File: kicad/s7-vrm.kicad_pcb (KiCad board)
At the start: 2 copper layers, 58.4 x 53 mm, 32 parts, among them J1 Conn_02x15_Row_Letter_First, Q1 Q_NPN_BEC, Q2 Q_NMOS_GDS, Q3 Q_NMOS_GDS, SW1 SW_DIP_x04, U1 NCP1579

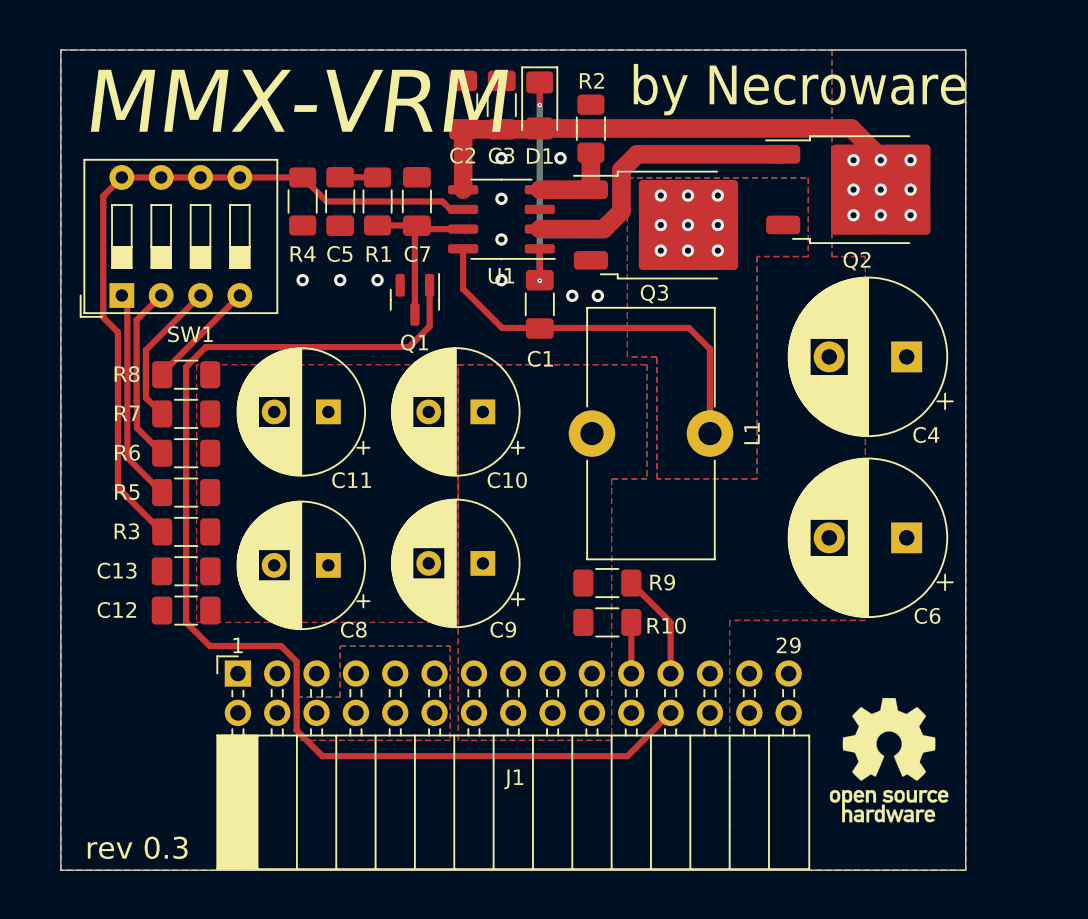
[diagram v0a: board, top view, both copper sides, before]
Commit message: Revision 0.4
- Added optional 1uF capacitors on input and output
- Increased the size of the inductor pins for SMD option
- Minor layout fixes
- Updated silk layer, logos etc.
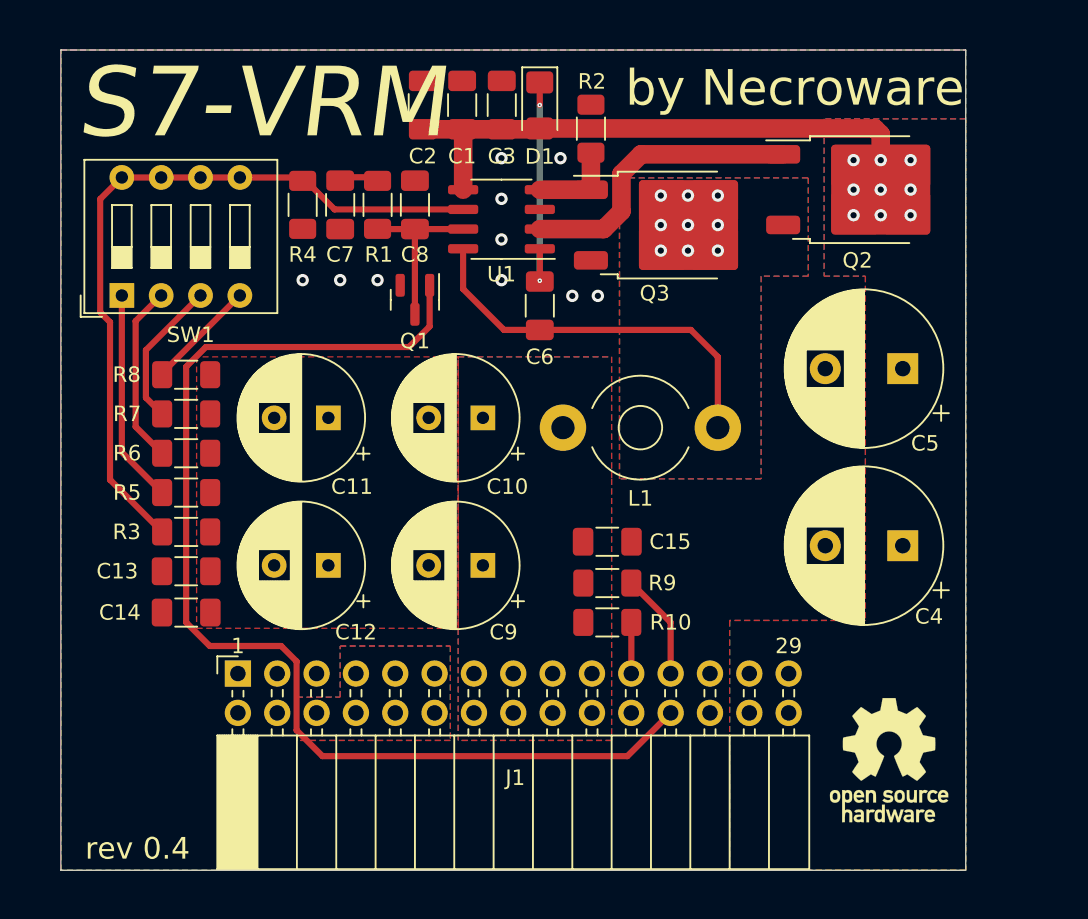
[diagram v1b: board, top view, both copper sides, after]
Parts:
- added C14: 4.7u, Capacitor_SMD:C_1206_3216Metric_Pad1.33x1.80mm_HandSolder, F.Cu at (129.0, 115.3)
- added C15: 10u, Capacitor_SMD:C_1206_3216Metric_Pad1.33x1.80mm_HandSolder, F.Cu at (156.2, 110.7)
- added G***: LOGO, s7-vrm:nw-logo, B.Cu at (143.1, 86.6)
- added G***: LOGO, s7-vrm:cc-by-sa-logo, B.Cu at (143.3, 96.1)
- C1: value 0.1u -> 10u
- C12: value 4.7u -> 1000u; footprint Capacitor_SMD:C_1206_3216Metric_Pad1.33x1.80mm_HandSolder -> Capacitor_THT:CP_Radial_D8.0mm_P3.50mm
- C5: value 22n -> 3300u; footprint Capacitor_SMD:C_1206_3216Metric_Pad1.33x1.80mm_HandSolder -> Capacitor_THT:CP_Radial_D10.0mm_P5.00mm
- C6: value 3300u -> 0.1u; footprint Capacitor_THT:CP_Radial_D10.0mm_P5.00mm -> Capacitor_SMD:C_1206_3216Metric_Pad1.33x1.80mm_HandSolder
- C7: value 220p -> 220nF
- C8: value 1000u -> 39p; footprint Capacitor_THT:CP_Radial_D8.0mm_P3.50mm -> Capacitor_SMD:C_1206_3216Metric_Pad1.33x1.80mm_HandSolder
- L1: value 2,5uH -> 2,5µH; footprint Inductor_THT:L_Toroid_Vertical_L16.0mm_W8.0mm_P7.62mm -> Inductor_THT:L_Toroid_Horizontal_D6.5mm_P10.00mm_Diameter7-5mm_Amidon-T25
- moved C5 37.9 mm to (175.3, 99.6), turned to 180 degrees
- moved C6 28.0 mm to (151.8, 95.5), turned to -90 degrees
- moved C8 23.9 mm to (143.8, 89.0), turned to 90 degrees
- moved C1 13.8 mm to (146.8, 82.5), turned to 90 degrees
- moved C4 12.2 mm to (175.3, 111.0)
- moved C12 9.64 mm to (138.2, 112.3)
- moved C7 4.96 mm to (138.9, 89.0), turned to -90 degrees
- moved C2 2.61 mm to (144.3, 82.5)
- moved L1 0.64 mm to (163.3, 103.4), turned to 180 degrees
- moved C10 0.38 mm to (148.2, 102.7)
- moved C11 0.38 mm to (138.2, 102.7)
- moved R1 0.22 mm to (141.4, 89.0)
- moved R4 0.22 mm to (136.5, 89.0)
- moved C9 0.13 mm to (148.2, 112.3)
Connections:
- C1 pad 1: /BST -> +5V
- C1 pad 2: /PHASE -> GND
- C5 pad 1: Net-(C5-Pad1) -> +5V
- C6 pad 1: +5V -> /BST
- C6 pad 2: GND -> /PHASE
- C7 pad 1: /COMP -> Net-(C7-Pad1)
- C8 pad 1: VCORE -> /COMP
- R1 pad 2: Net-(C5-Pad1) -> Net-(C7-Pad1)
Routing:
- net +5V: track 33.7 -> 37.2 mm
- net Net-(C7-Pad1): track 0.00 -> 2.42 mm
- net Net-(C5-Pad1): track 2.42 -> 0.00 mm
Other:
- board text added: "${TITLE}"
- board text removed: "MMX-VRM"

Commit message: Updated logos, readme and photo
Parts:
- G***: moved to F.Cu
- moved G*** 32.8 mm to (126.2, 124.2), turned to 90 degrees
- moved G*** 26.6 mm to (169.6, 88.6)
- moved REF** 1.66 mm to (174.5, 123.2)

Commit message: Layout improvements
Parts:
- R3: value 3K -> 1K
- R4: value 1K -> 3K
- moved R4 22.4 mm to (129.0, 110.1), turned to 180 degrees
- moved R3 22.4 mm to (136.4, 89.0), turned to -90 degrees
- moved C13 2.67 mm to (129.0, 115.3)
- moved C14 2.60 mm to (129.0, 112.7)
- moved C1 2.54 mm to (144.3, 82.5)
- moved C2 2.54 mm to (146.8, 82.5)
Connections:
- R3 pad 1: VCORE -> FB
- R3 pad 2: FB -> GND
- R4 pad 1: FB -> VCORE
- R4 pad 2: GND -> FB
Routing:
- net /PHASE: track 25.4 -> 23.3 mm

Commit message: Fixed BOM in readme, fixed part numbers in schematics
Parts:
- C7: value 220nF -> 220n
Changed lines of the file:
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@@
         (effects (font (size 1 1) (thickness 0.15)))
     )
-    (fp_text value "220nF" (at 0 1.85 90) (layer "F.Fab")
+    (fp_text value "220n" (at 0 1.85 90) (layer "F.Fab")
         (effects (font (size 1 1) (thickness 0.15)))
     )

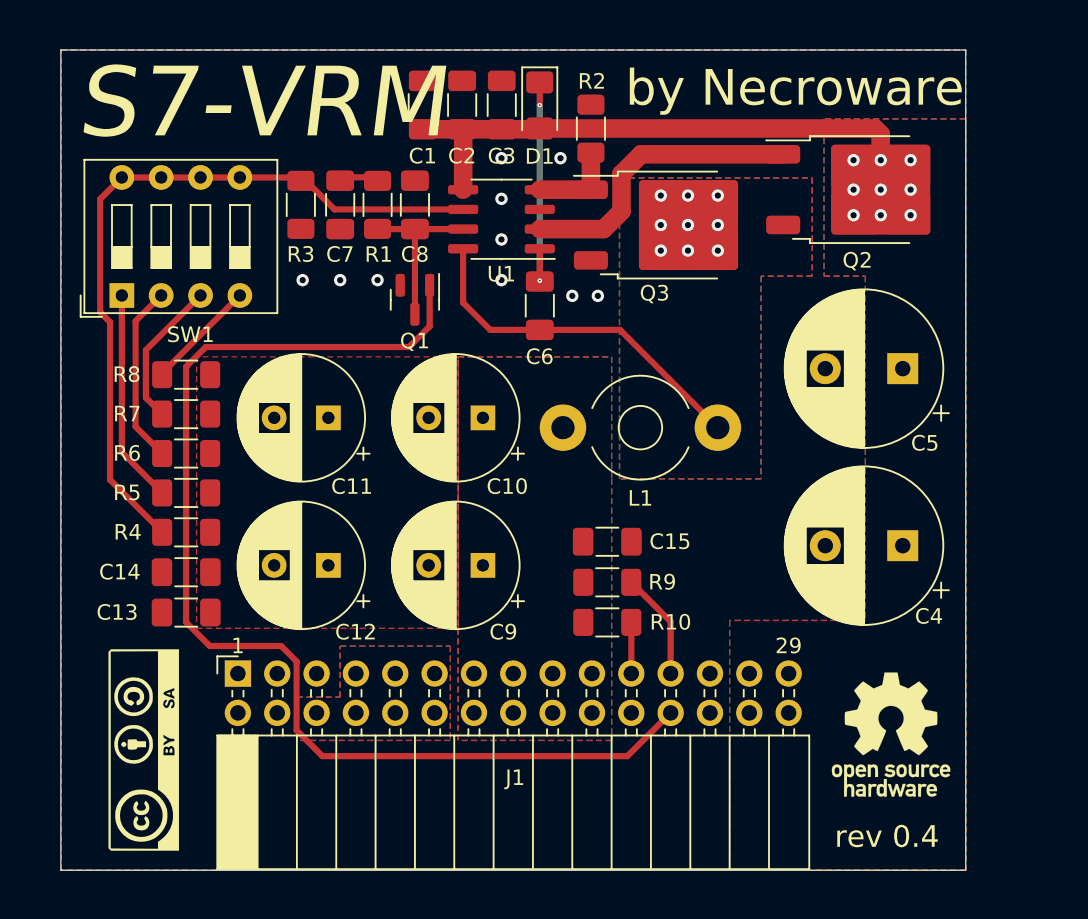
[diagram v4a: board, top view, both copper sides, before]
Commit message: Layout improvements, added slits for the clips
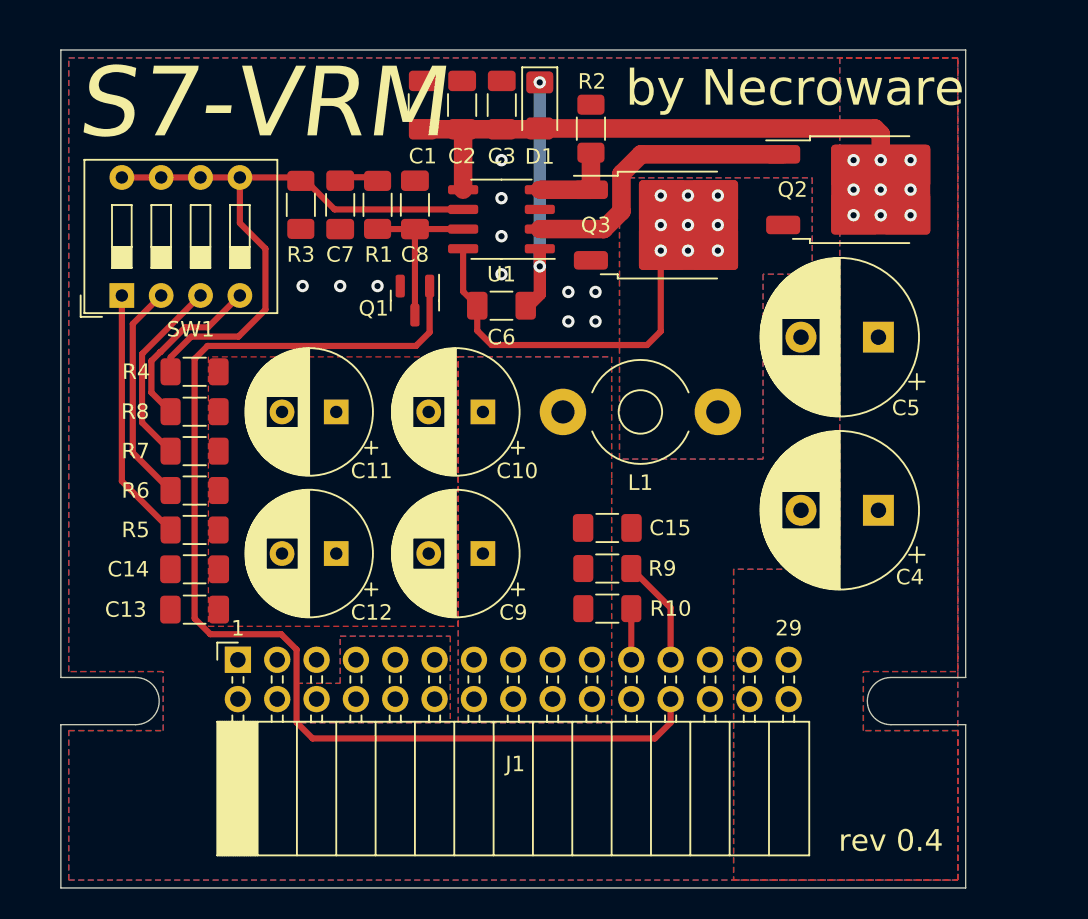
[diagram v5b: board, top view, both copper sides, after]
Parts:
- removed the G*** at (169.6, 88.6)
- C13, C3, C6: value 0.1u -> 100n
- G***, REF**: moved to B.Cu
- moved G*** 55.2 mm to (171.3, 92.3), turned to 180 degrees
- moved REF** 38.6 mm to (171.3, 84.7), turned to 180 degrees
- moved R4 10.4 mm to (129.5, 99.8)
- moved C4 2.77 mm to (173.7, 108.7)
- moved C5 2.57 mm to (173.7, 97.5)
- moved C6 2.47 mm to (149.4, 95.5), turned to 180 degrees
- moved R5 2.45 mm to (129.5, 110.0)
- moved R6 2.45 mm to (129.5, 107.4)
- moved R7 2.45 mm to (129.5, 104.9)
- moved R8 2.45 mm to (129.5, 102.3)
- moved L1 1.02 mm to (163.3, 102.4)
- moved C12 0.92 mm to (138.7, 111.5)
- moved C15 0.89 mm to (156.2, 109.9)
- moved J1 0.89 mm to (132.3, 118.4)
- moved R10 0.89 mm to (156.2, 115.1)
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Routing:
- net FB: track 48.0 -> 40.4 mm
- net Net-(R8-Pad2): track 7.19 -> 11.3 mm
- net Net-(R7-Pad2): track 9.54 -> 12.4 mm
- net Net-(R6-Pad2): track 11.6 -> 14.4 mm
- net Net-(R5-Pad2): track 13.8 -> 16.4 mm
- net /BST: track 14.8 -> 15.9 mm
- net GND: vias 10 -> 11
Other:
- board size 58.4 x 53 mm -> 58.4 x 54.1 mm

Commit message: Updated parts and documenttion
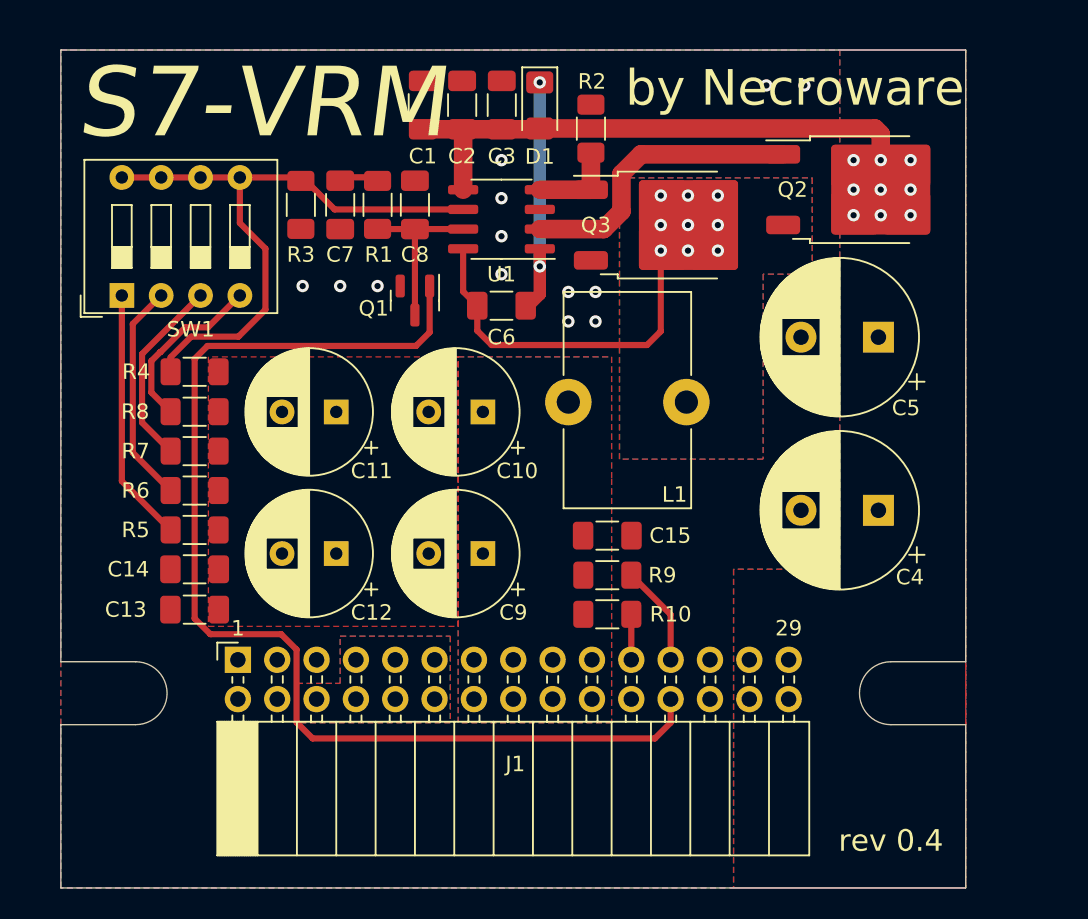
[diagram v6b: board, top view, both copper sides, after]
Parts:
- L1: value 2,5µH -> 3,3u; footprint Inductor_THT:L_Toroid_Horizontal_D6.5mm_P10.00mm_Diameter7-5mm_Amidon-T25 -> Inductor_THT:L_Toroid_Vertical_L16.0mm_W8.0mm_P7.62mm
- moved L1 2.13 mm to (161.3, 101.7), turned to -90 degrees
- moved C15 0.49 mm to (156.2, 110.3)
- moved R9 0.43 mm to (156.2, 112.9)
- moved R10 0.37 mm to (156.2, 115.4)
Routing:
- net GND: vias 11 -> 13
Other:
- outline, holes or cut-outs redrawn

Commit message: Increase PCB width slightly
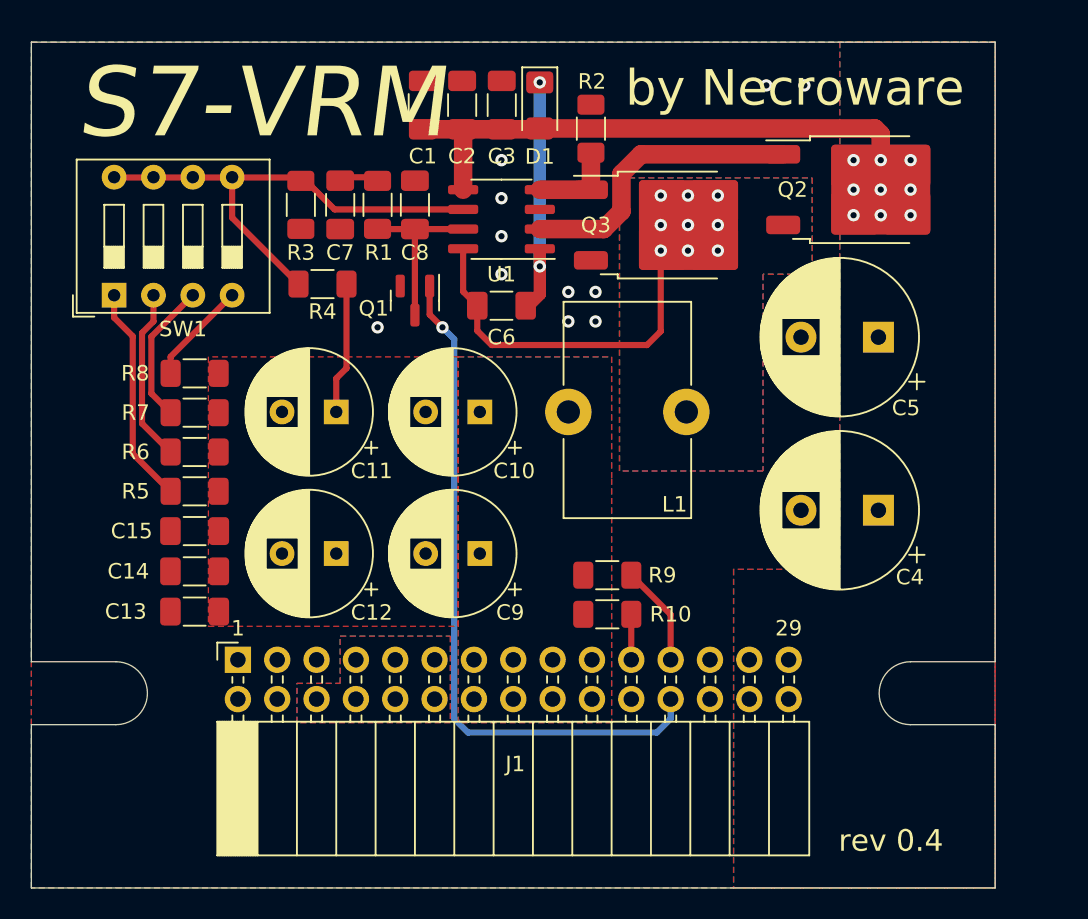
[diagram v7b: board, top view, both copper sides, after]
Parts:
- moved C15 26.6 mm to (129.5, 110.1), turned to 180 degrees
- moved R4 10.0 mm to (137.8, 94.1)
- moved R5 2.49 mm to (129.5, 107.5)
- moved R6 2.49 mm to (129.5, 104.9)
- moved R7 2.48 mm to (129.5, 102.4)
- moved R8 2.48 mm to (129.5, 99.9)
- moved L1 0.63 mm to (161.3, 102.4)
- moved SW1 0.50 mm to (124.3, 94.8)
- moved C10 0.20 mm to (148.0, 102.4)
- moved C9 0.20 mm to (148.0, 111.5)
- moved C14 0.13 mm to (129.5, 112.7)
- moved C13 0.13 mm to (129.5, 115.3)
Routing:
- net DISABLE: track 74.3 -> 44.6 mm, vias 0 -> 1
- net VCORE: track 0.00 -> 8.53 mm
- net FB: track 40.4 -> 32.1 mm
- net Net-(R8-Pad2): track 11.3 -> 6.69 mm
- net Net-(R6-Pad2): track 14.4 -> 11.2 mm
- net Net-(R7-Pad2): track 12.4 -> 9.21 mm
- net Net-(R5-Pad2): track 16.4 -> 14.2 mm
- net GND: vias 13 -> 11
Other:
- board size 58.4 x 54.1 mm -> 62.2 x 54.6 mm

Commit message: Take shorter input capacitor
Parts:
- C4, C5: value 3300u -> 2200u
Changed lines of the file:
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@@
     (descr "CP, Radial series, Radial, pin pitch=5.00mm, , diameter=10mm, Electrolytic Capacitor")
     (tags "CP Radial series Radial pin pitch 5.00mm  diameter 10mm Electrolytic Capacitor")
-    (property "LCSC" "C407862")
+    (property "LCSC" "C407963")
     (property "Sheetfile" "s7-vrm.kicad_sch")
     (property "Sheetname" "")
@@
         (effects (font (size 1 1) (thickness 0.15)))
     )
-    (fp_text value "3300u" (at 2.54 2.54) (layer "F.Fab")
+    (fp_text value "2200u" (at 2.54 2.54) (layer "F.Fab")
         (effects (font (size 1 1) (thickness 0.15)))
     )
@@
     (descr "CP, Radial series, Radial, pin pitch=5.00mm, , diameter=10mm, Electrolytic Capacitor")
     (tags "CP Radial series Radial pin pitch 5.00mm  diameter 10mm Electrolytic Capacitor")
-    (property "LCSC" "C407862")
+    (property "LCSC" "C407963")
     (property "Sheetfile" "s7-vrm.kicad_sch")
     (property "Sheetname" "")
@@
         (effects (font (size 1 1) (thickness 0.15)))
     )
-    (fp_text value "3300u" (at 2.54 2.54) (layer "F.Fab")
-        (effects (font (size 1 1) (thickness 0.15)))
-    )
+    (fp_text value "2200u" (at 2.54 2.54) (layer "F.Fab")
+        (effects (font (size 1 1) (thickness 0.15)))
+    )
